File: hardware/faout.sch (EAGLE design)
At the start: 165 parts, among them IC2 MT48LC8M16A2, Q1 12MHz, Q2 MUN2214T1, Q3 MUN2214T1, Q4 ASFL, SW1 SMD_TACT_SWITCH, SW2 SMD_TACT_SWITCH, SW3 SMD_TACT_SWITCH, U1 93LC46BT-I/OT, U10 REF102AU, U11 DAC8811DGK, U12 REF102AU, U13 DAC8811DGK, U14 ADR435ARZ, U15 AD8627AKSZ-R2, U16 OPA2277UA/2K5E4, U17 OPA2277UA/2K5E4, U18 MCP1700T-2502E/TT, U19 AD7980ARMZ, U2 LM3480IM3-3.3, U3 L7812ACV, U4 L7912ACV, U5 LM3671MF-3.3, U6 LM3671MF-1.2, U7 M25PE16, U8 6SLX9TQG144, U9 AD8220ARMZ

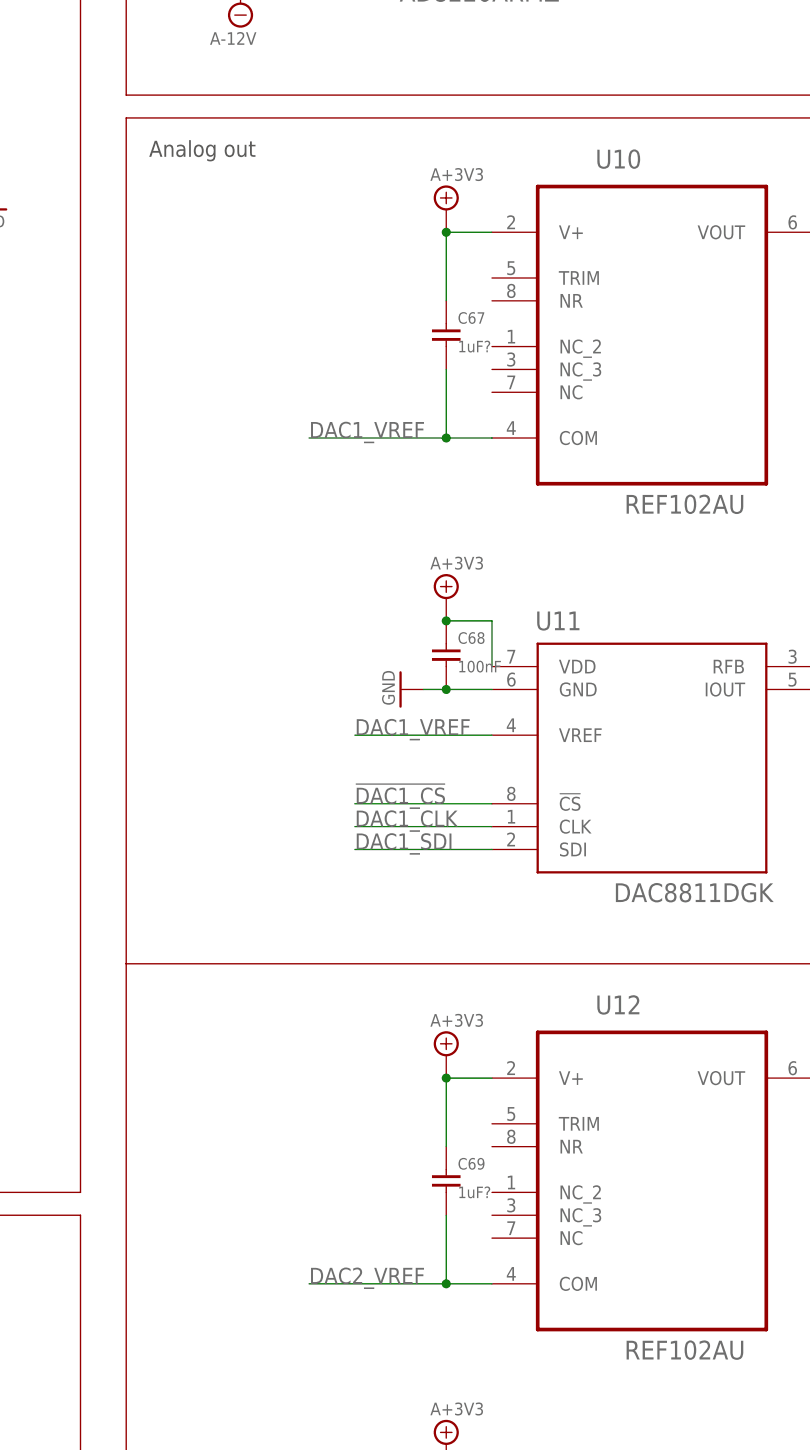
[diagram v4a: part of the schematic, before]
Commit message: Fix DAC voltage ref oscillations in next board version.
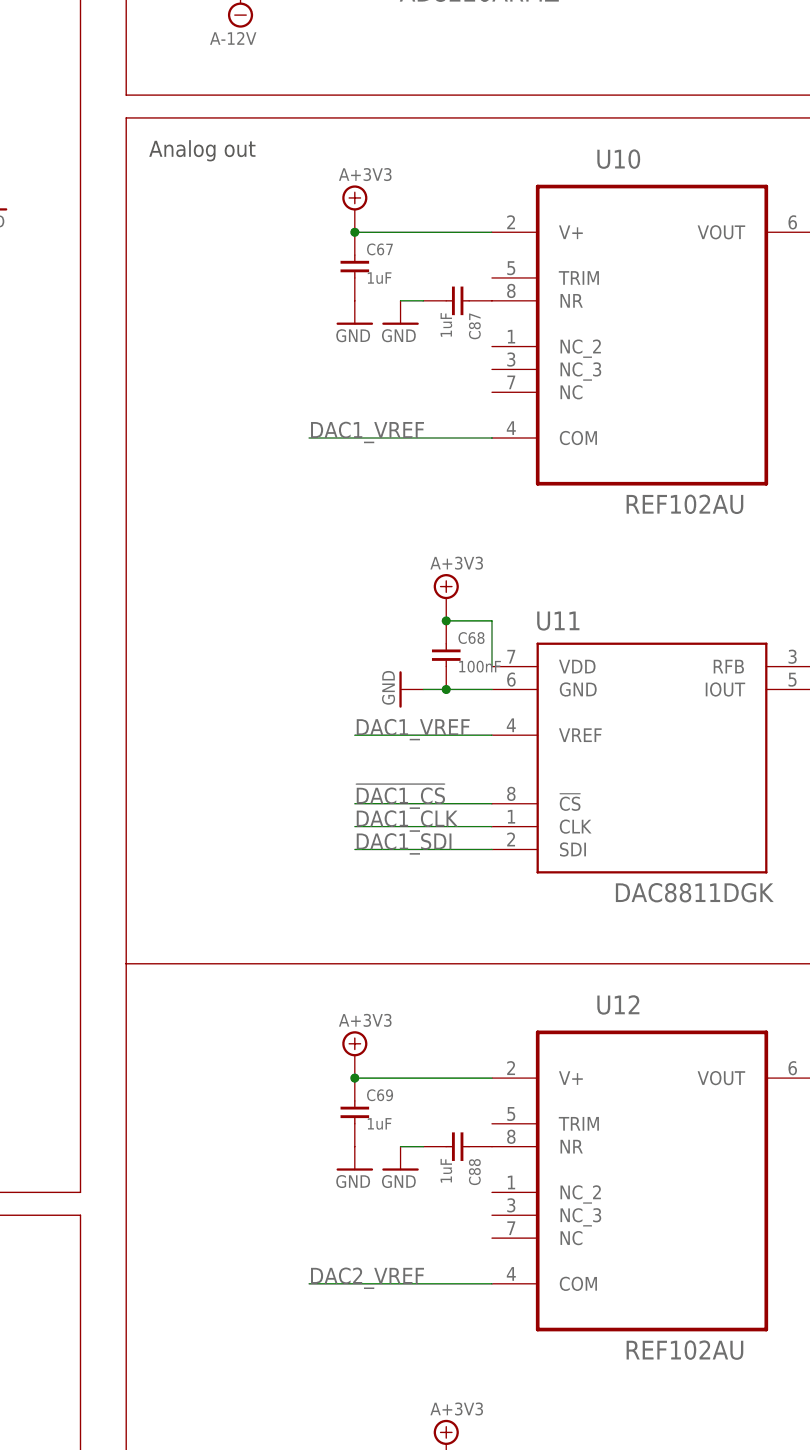
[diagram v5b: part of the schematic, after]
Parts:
- added C87, C88: 1uF, faout:C_EU0603
- C67, C69: value 1uF? -> 1uF
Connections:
- new net N$17: C87.P$1, U10.NR
- new net N$27: C88.P$1, U12.NR
- net DAC1_VREF: no longer C67.P$2
- net DAC2_VREF: no longer C69.P$2
- net GND: now also C67.P$2, C69.P$2, C87.P$2, C88.P$2
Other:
- moved on the sheet: C67, C69
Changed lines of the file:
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@@
 <part name="C78" library="faout" deviceset="C_EU" device="0603" value="1nF"/>
 <part name="R29" library="faout" deviceset="R_EU" device="0603" value="2k"/>
-<part name="C67" library="faout" deviceset="C_EU" device="0603" value="1uF?">
+<part name="C67" library="faout" deviceset="C_EU" device="0603" value="1uF">
 <attribute name="OC_FARNELL" value="1759409"/>
 </part>
@@
 <part name="C79" library="faout" deviceset="C_EU" device="0603" value="1nF"/>
 <part name="R30" library="faout" deviceset="R_EU" device="0603" value="2k"/>
-<part name="C69" library="faout" deviceset="C_EU" device="0603" value="1uF?">
+<part name="C69" library="faout" deviceset="C_EU" device="0603" value="1uF">
 <attribute name="OC_FARNELL" value="1759409"/>
 </part>
@@
 <part name="GND_PWR81" library="Bogdan_Commons" deviceset="GND" device=""/>
 <part name="U7" library="faout" deviceset="M25PE16" device=""/>
+<part name="C87" library="faout" deviceset="C_EU" device="0603" value="1uF">
+<attribute name="OC_FARNELL" value="1759409"/>
+</part>
+<part name="GND_PWR82" library="faout" deviceset="GND" device=""/>
+<part name="GND_PWR83" library="faout" deviceset="GND" device=""/>
+<part name="GND_PWR84" library="faout" deviceset="GND" device=""/>
+<part name="C88" library="faout" deviceset="C_EU" device="0603" value="1uF">
+<attribute name="OC_FARNELL" value="1759409"/>
+</part>
+<part name="GND_PWR85" library="faout" deviceset="GND" device=""/>
 </parts>
 <sheets>
@@
 <instance part="C78" gate="G$1" x="378.46" y="-129.54"/>
 <instance part="R29" gate="G$1" x="373.38" y="-127"/>
-<instance part="C67" gate="G$1" x="327.66" y="-137.16">
-<attribute name="OC_FARNELL" x="327.66" y="-137.16" size="1.778" layer="96" display="off"/>
+<instance part="C67" gate="G$1" x="317.5" y="-129.54">
+<attribute name="OC_FARNELL" x="317.5" y="-129.54" size="1.778" layer="96" display="off"/>
 </instance>
 <instance part="C68" gate="G$1" x="327.66" y="-172.72">
@@
 <instance part="C79" gate="G$1" x="378.46" y="-223.52"/>
 <instance part="R30" gate="G$1" x="373.38" y="-220.98"/>
-<instance part="C69" gate="G$1" x="327.66" y="-231.14">
-<attribute name="OC_FARNELL" x="327.66" y="-231.14" size="1.778" layer="96" display="off"/>
+<instance part="C69" gate="G$1" x="317.5" y="-223.52">
+<attribute name="OC_FARNELL" x="317.5" y="-223.52" size="1.778" layer="96" display="off"/>
 </instance>
 <instance part="C70" gate="G$1" x="327.66" y="-266.7">
@@
 <instance part="GND_PWR55" gate="A" x="304.8" y="-71.12"/>
 <instance part="GND_PWR56" gate="A" x="304.8" y="-88.9" rot="R180"/>
-<instance part="A+12V_PWR3" gate="G$1" x="327.66" y="-124.46"/>
+<instance part="A+12V_PWR3" gate="G$1" x="317.5" y="-124.46"/>
 <instance part="A+12V_PWR5" gate="G$1" x="426.72" y="-167.64"/>
 <instance part="U$3" gate="G$1" x="426.72" y="-193.04"/>
@@
 <instance part="U$5" gate="G$1" x="436.88" y="-149.86"/>
 <instance part="A+12V_PWR4" gate="G$1" x="327.66" y="-167.64"/>
-<instance part="U$7" gate="G$1" x="327.66" y="-218.44"/>
+<instance part="U$7" gate="G$1" x="317.5" y="-218.44"/>
 <instance part="U$8" gate="G$1" x="327.66" y="-261.62"/>
 <instance part="U$9" gate="G$1" x="424.18" y="-261.62"/>
@@
 <instance part="GND_PWR81" gate="A" x="83.82" y="55.88"/>
 <instance part="U7" gate="G$1" x="228.6" y="-279.4"/>
+<instance part="C87" gate="G$1" x="330.2" y="-134.62" rot="R270">
+<attribute name="OC_FARNELL" x="330.2" y="-134.62" size="1.778" layer="96" rot="R270" display="off"/>
+</instance>
+<instance part="GND_PWR82" gate="A" x="317.5" y="-137.16"/>
+<instance part="GND_PWR83" gate="A" x="322.58" y="-137.16"/>
+<instance part="GND_PWR84" gate="A" x="317.5" y="-231.14"/>
+<instance part="C88" gate="G$1" x="330.2" y="-228.6" rot="R270">
+<attribute name="OC_FARNELL" x="330.2" y="-228.6" size="1.778" layer="96" rot="R270" display="off"/>
+</instance>
+<instance part="GND_PWR85" gate="A" x="322.58" y="-231.14"/>
 </instances>
 <busses>
@@
 <pinref part="GND_PWR81" gate="A" pin="GND"/>
 </segment>
+<segment>
+<pinref part="C67" gate="G$1" pin="P$2"/>
+<pinref part="GND_PWR82" gate="A" pin="GND"/>
+</segment>
+<segment>
+<pinref part="C87" gate="G$1" pin="P$2"/>
+<pinref part="GND_PWR83" gate="A" pin="GND"/>
+<wire x1="322.58" y1="-134.62" x2="325.12" y2="-134.62" width="0.1524" layer="91"/>
+</segment>
+<segment>
+<pinref part="C69" gate="G$1" pin="P$2"/>
+<pinref part="GND_PWR84" gate="A" pin="GND"/>
+</segment>
+<segment>
+<pinref part="C88" gate="G$1" pin="P$2"/>
+<pinref part="GND_PWR85" gate="A" pin="GND"/>
+<wire x1="322.58" y1="-228.6" x2="325.12" y2="-228.6" width="0.1524" layer="91"/>
+</segment>
 </net>
 <net name="N$1" class="0">
@@
 </segment>
 <segment>
-<wire x1="312.42" y1="-149.86" x2="327.66" y2="-149.86" width="0.1524" layer="91"/>
+<wire x1="312.42" y1="-149.86" x2="332.74" y2="-149.86" width="0.1524" layer="91"/>
 <pinref part="U10" gate="A" pin="COM"/>
 <label x="312.42" y="-149.86" size="1.778" layer="95"/>
-<pinref part="C67" gate="G$1" pin="P$2"/>
-<wire x1="327.66" y1="-149.86" x2="332.74" y2="-149.86" width="0.1524" layer="91"/>
-<wire x1="327.66" y1="-142.24" x2="327.66" y2="-149.86" width="0.1524" layer="91"/>
-<junction x="327.66" y="-149.86"/>
 </segment>
 <segment>
@@
 </segment>
 <segment>
-<wire x1="312.42" y1="-243.84" x2="327.66" y2="-243.84" width="0.1524" layer="91"/>
+<wire x1="312.42" y1="-243.84" x2="332.74" y2="-243.84" width="0.1524" layer="91"/>
 <pinref part="U12" gate="A" pin="COM"/>
 <label x="312.42" y="-243.84" size="1.778" layer="95"/>
-<pinref part="C69" gate="G$1" pin="P$2"/>
-<wire x1="327.66" y1="-243.84" x2="332.74" y2="-243.84" width="0.1524" layer="91"/>
-<wire x1="327.66" y1="-236.22" x2="327.66" y2="-243.84" width="0.1524" layer="91"/>
-<junction x="327.66" y="-243.84"/>
 </segment>
 <segment>
@@
 <pinref part="U10" gate="A" pin="V+"/>
 <pinref part="C67" gate="G$1" pin="P$1"/>
-<wire x1="327.66" y1="-127" x2="332.74" y2="-127" width="0.1524" layer="91"/>
-<wire x1="327.66" y1="-134.62" x2="327.66" y2="-127" width="0.1524" layer="91"/>
-<junction x="327.66" y="-127"/>
+<wire x1="317.5" y1="-127" x2="332.74" y2="-127" width="0.1524" layer="91"/>
+<junction x="317.5" y="-127"/>
 <pinref part="A+12V_PWR3" gate="G$1" pin="A+3V3"/>
 </segment>
@@
 <pinref part="U12" gate="A" pin="V+"/>
 <pinref part="C69" gate="G$1" pin="P$1"/>
-<wire x1="327.66" y1="-220.98" x2="332.74" y2="-220.98" width="0.1524" layer="91"/>
-<wire x1="327.66" y1="-228.6" x2="327.66" y2="-220.98" width="0.1524" layer="91"/>
-<junction x="327.66" y="-220.98"/>
+<wire x1="317.5" y1="-220.98" x2="332.74" y2="-220.98" width="0.1524" layer="91"/>
+<junction x="317.5" y="-220.98"/>
 <pinref part="U$7" gate="G$1" pin="A+3V3"/>
 </segment>
@@
 </segment>
 </net>
+<net name="N$17" class="0">
+<segment>
+<pinref part="U10" gate="A" pin="NR"/>
+<pinref part="C87" gate="G$1" pin="P$1"/>
+</segment>
+</net>
+<net name="N$27" class="0">
+<segment>
+<pinref part="U12" gate="A" pin="NR"/>
+<pinref part="C88" gate="G$1" pin="P$1"/>
+</segment>
+</net>

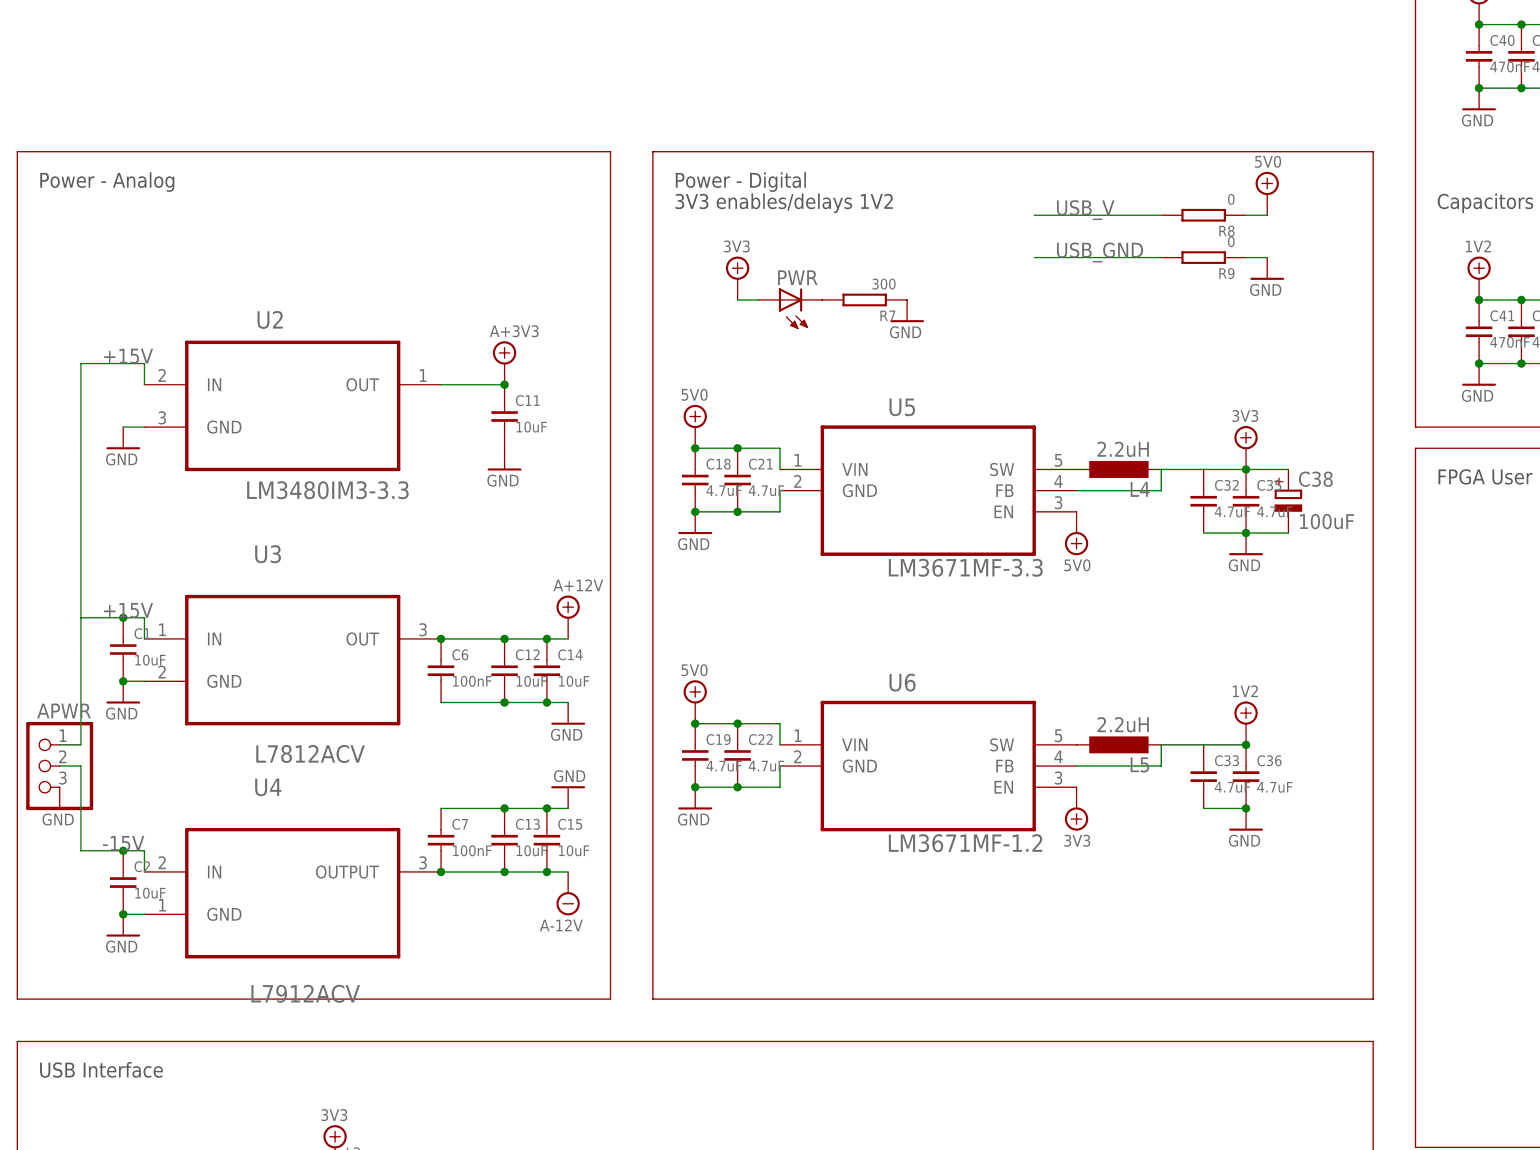
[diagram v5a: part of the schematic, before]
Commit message: Larger SMD pads and optional capacitors.
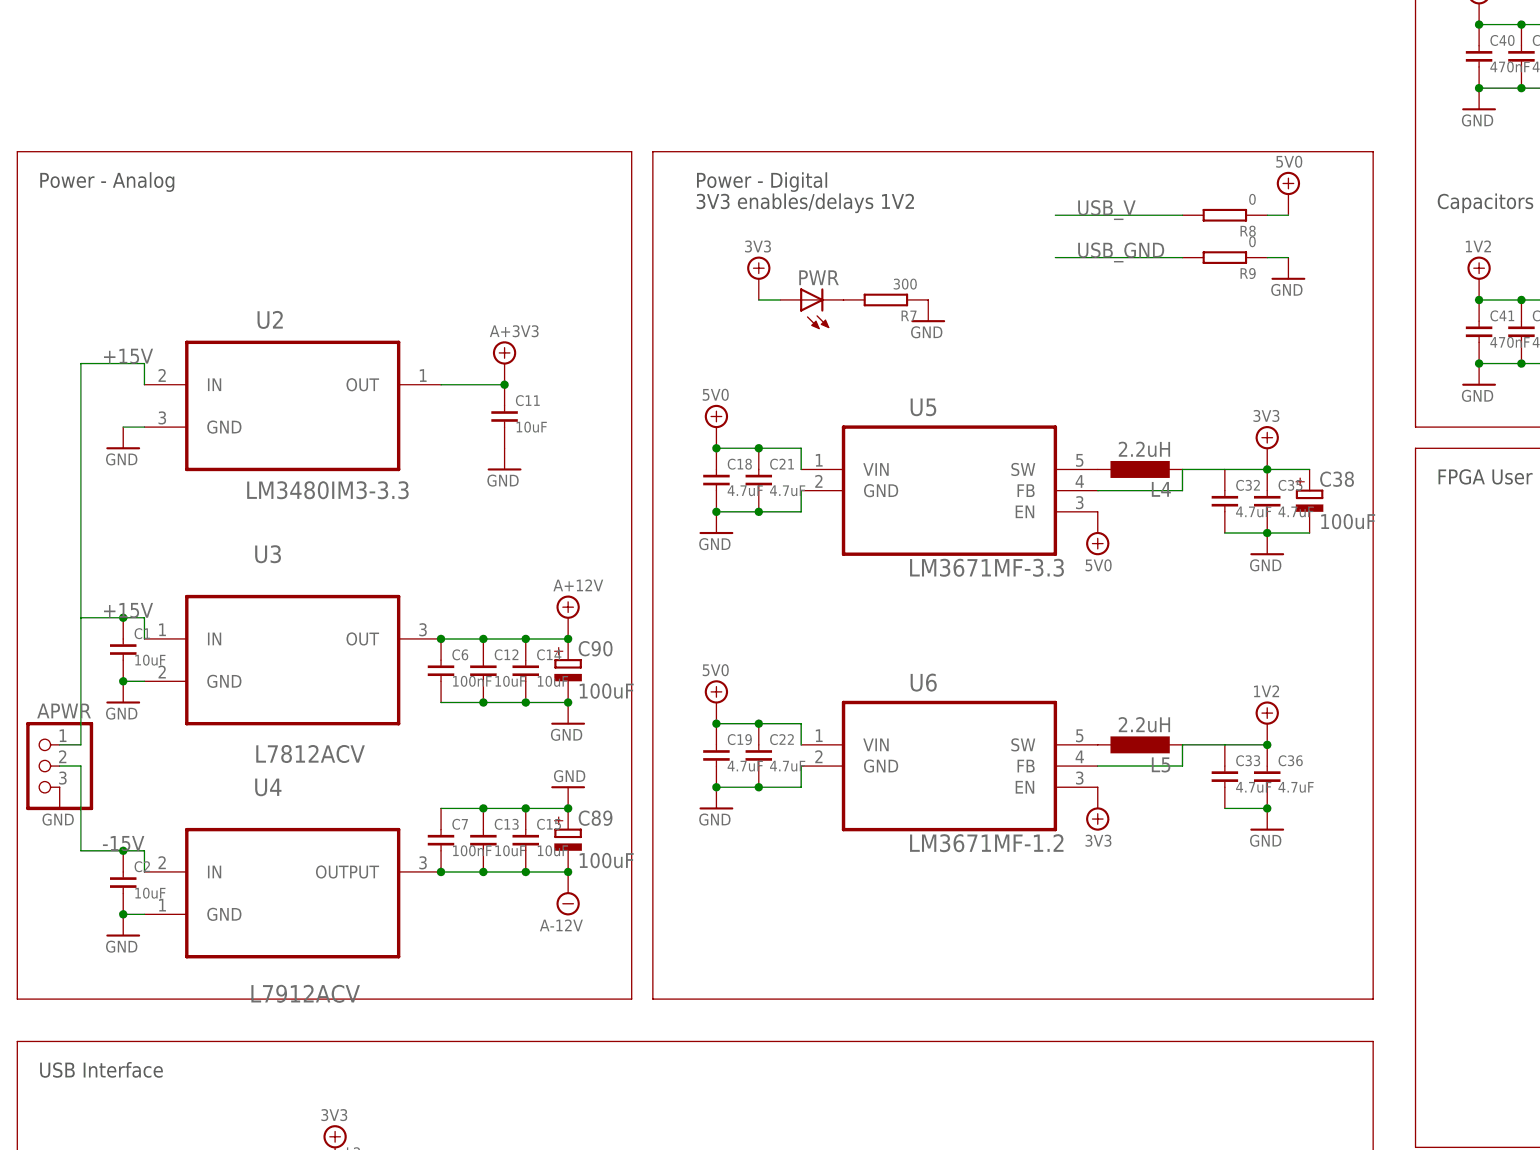
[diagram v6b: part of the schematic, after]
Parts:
- added C89, C90: 100uF, rcl:CPOL-EUE
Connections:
- net A+12V: now also C90.+
- net A-12V: now also C89.-
- net GND: now also C89.+, C90.-
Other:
- moved on the sheet: C12, C13, C14, C15, C18, C19, C21, C22, C32, C33, C35, C36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
